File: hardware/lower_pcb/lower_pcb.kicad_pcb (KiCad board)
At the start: 2 copper layers, 88 x 88 mm, 22 parts, among them J1 USB-C, J2 JST-PH-2P, J3 FPC-6P-0.5mm, J4 Alps-RKJXV, SW1 MSK-12C02, SW2 BOOT-SW, SW3 RESET-SW, U1 XIAO-ESP32S3, U3 AP2112K-3.3V

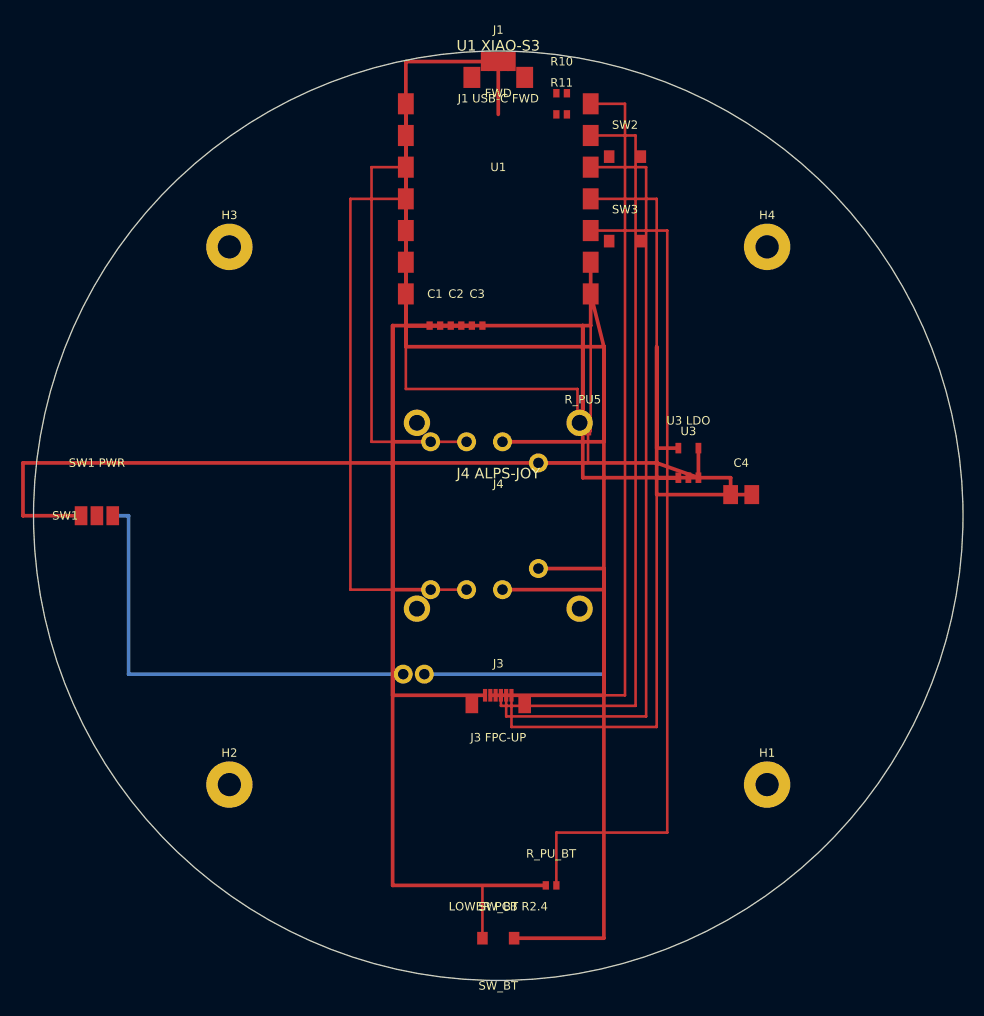
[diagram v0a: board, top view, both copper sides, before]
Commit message: feat: simplify to 2-layer single-sided routing, all traces on F.Cu
- All signal and power traces moved to F.Cu only
- No vias anywhere - eliminates layer-change complexity
- B.Cu = solid GND pour only (add zone fill in KiCad)
- BAT_PLUS routed on F.Cu around south edge to SW1
- J2 battery and J5 FPC connectors both on F.Cu (THT accessible both sides)
- Lower PCB: 88 segments (was 91 with vias/B.Cu traces)
- Upper PCB: 42 segments (was 52 with B.Cu vias)
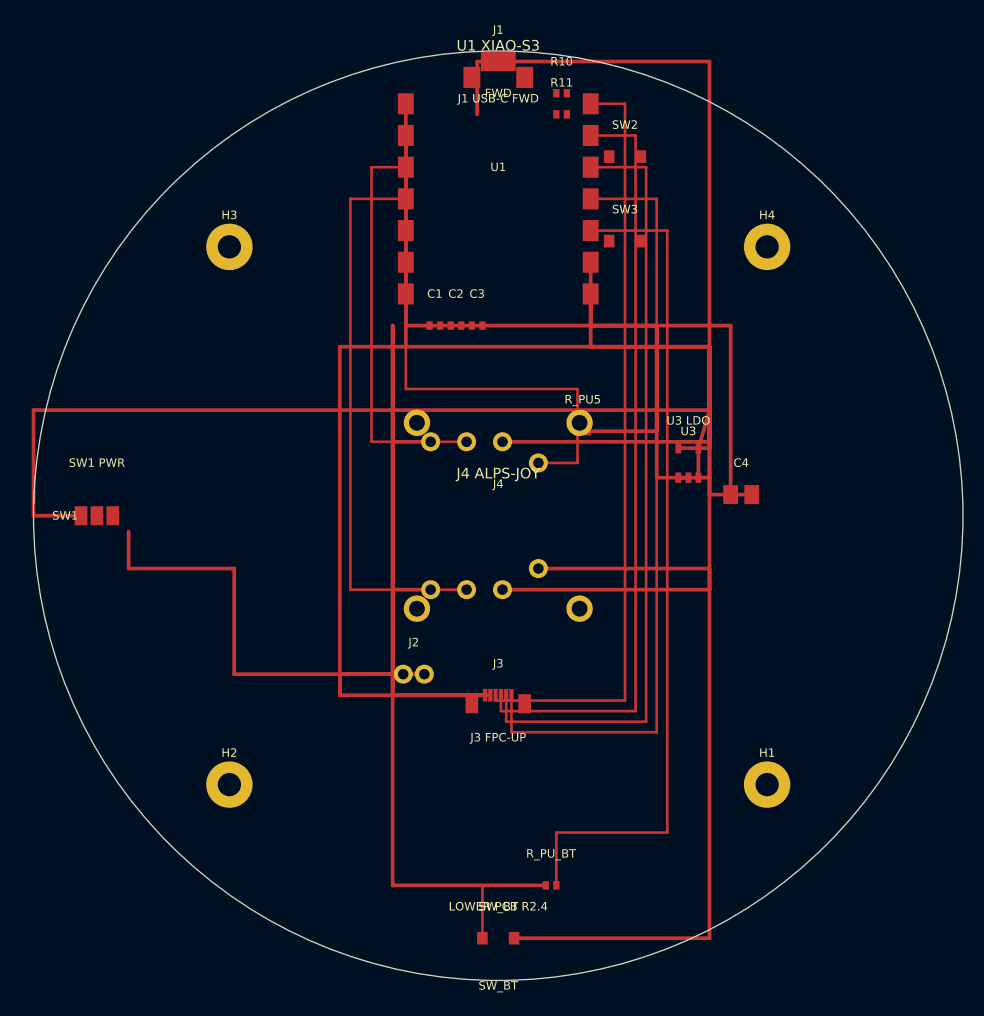
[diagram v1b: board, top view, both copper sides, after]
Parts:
- J2: moved to F.Cu
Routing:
- net GND: track 254.4 -> 349.3 mm, vias 1 -> 0
- net 3V3: track 210.9 -> 233.3 mm
- net JOY_SW: track 60.2 -> 42.0 mm
- net SW_OUT: track 77.5 -> 85.1 mm
- net BAT_PLUS: track 42.5 -> 39.5 mm
- net BTN_R: track 72.0 -> 73.0 mm
- net BTN_L: track 71.5 -> 72.5 mm
- net BTN_FW: track 73.0 -> 74.0 mm
- net BTN_BK: track 72.5 -> 73.5 mm
- net VBUS: track 6.25 -> 5.75 mm

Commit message: fix: rewrite add_traces.py with verified pad coordinates
All trace endpoints now match exact footprint pad positions:
- XIAO: 7 left pads + 7 right pads at correct absolute coords
- J4 Alps RKJXV: X/Y wipers, CCW(3V3), CW(GND), SW, mounting legs
- J3/J5 FPC: 6 signal pads at 0.5mm pitch
- U3 LDO SOT-23-5: pin1-5 exact positions
- J2 JST-PH: pin1(BAT+), pin2(GND)
- SW1 SPDT: COM/NO at correct rotated positions
- SW4/SW5 GM8.0: NO(-5.08)/COM(0)/NC(+5.08) horizontal row
- SW6/SW7 SKHLLBA010: 4 holes at +-3.25mm square
- R1-R4, R_PU5, R_PU_BT, C1-C4 pull-ups and decoupling
- 573 lower + 239 upper trace segments, all F.Cu, zero vias
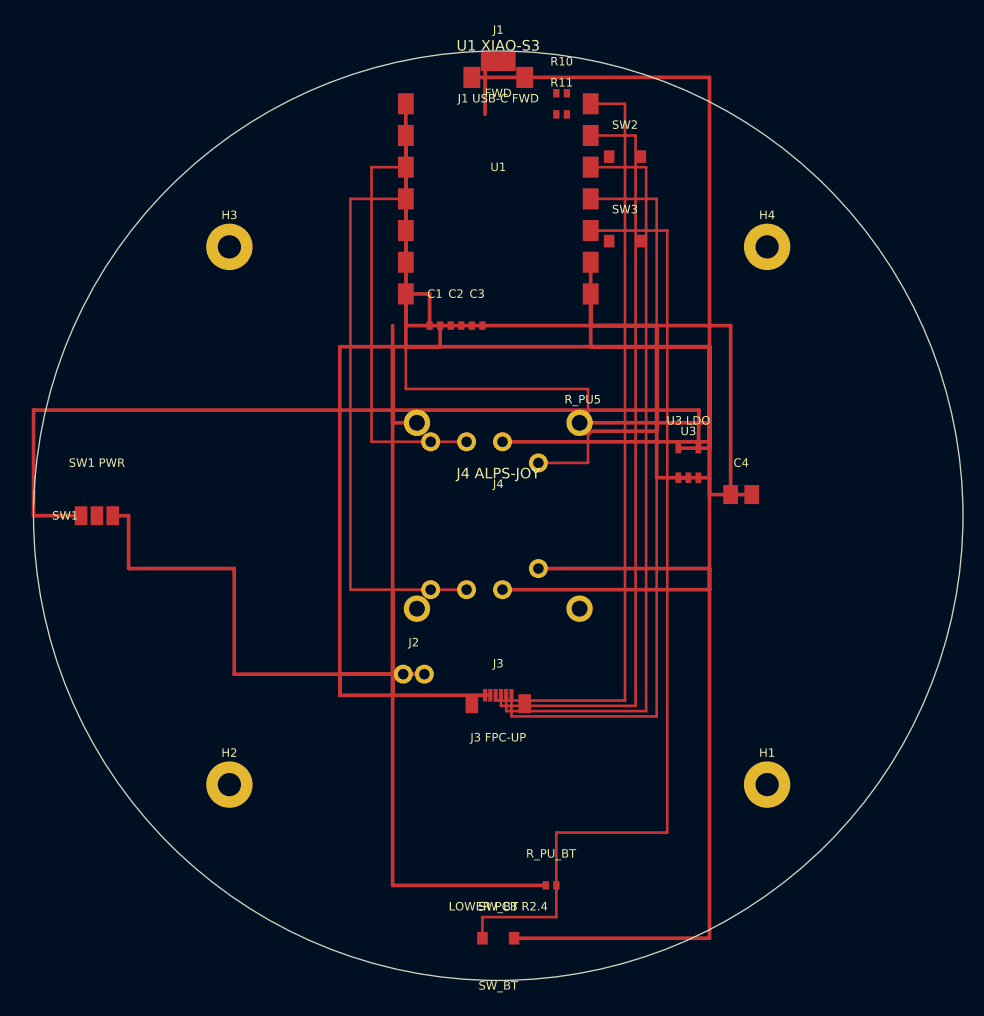
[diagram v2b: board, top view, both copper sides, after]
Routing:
- net GND: track 349.3 -> 385.1 mm
- net 3V3: track 233.3 -> 197.7 mm
- net SW_OUT: track 85.1 -> 81.1 mm
- net BTN_FW: track 74.0 -> 71.0 mm
- net BAT_PLUS: track 39.5 -> 42.5 mm
- net JOY_SW: track 42.0 -> 44.0 mm
- net BTN_BK: track 73.5 -> 71.5 mm
- net BT_SYNC: track 90.8 -> 91.8 mm
- net BTN_R: track 73.0 -> 72.0 mm
- net VBUS: track 5.75 -> 5.00 mm

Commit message: feat: replace generic XIAO with Seeed XIAO ESP32-S3 Sense footprint
- Correct castellated pad pitch: 2.54mm (was wrong 3.0mm)
- Correct pin count: 8 per side (was 7)
- GPIO remapping to actual XIAO ESP32-S3 Sense pin names:
    JOY_X  → D0/A0 (GPIO1)
    JOY_Y  → D1/A1 (GPIO2)
    JOY_SW → D2/A2 (GPIO3)
    ADC_BAT→ D3/A3 (GPIO4)
    BTN_L  → D10/MOSI (GPIO10)
    BTN_R  → D9/MISO (GPIO9)
    BTN_BK → D8/SCK (GPIO8)
    BTN_FW → D7/RX (GPIO44)
    BT_SYNC→ D6/TX (GPIO43)
    VIN/VBAT→ right pad 1 (from SW1 → J2 LiPo)
- Removed: J1 USB-C, U3 AP2112K LDO, R10/R11 CC, C4
  (all redundant — XIAO has built-in USB-C, charging IC, 3.3V LDO)
- Net list simplified: VBUS/BAT_PLUS/SW_OUT removed, VBAT added
- SW1 now switches VBAT directly to XIAO VIN
- Lower PCB rev 3.0
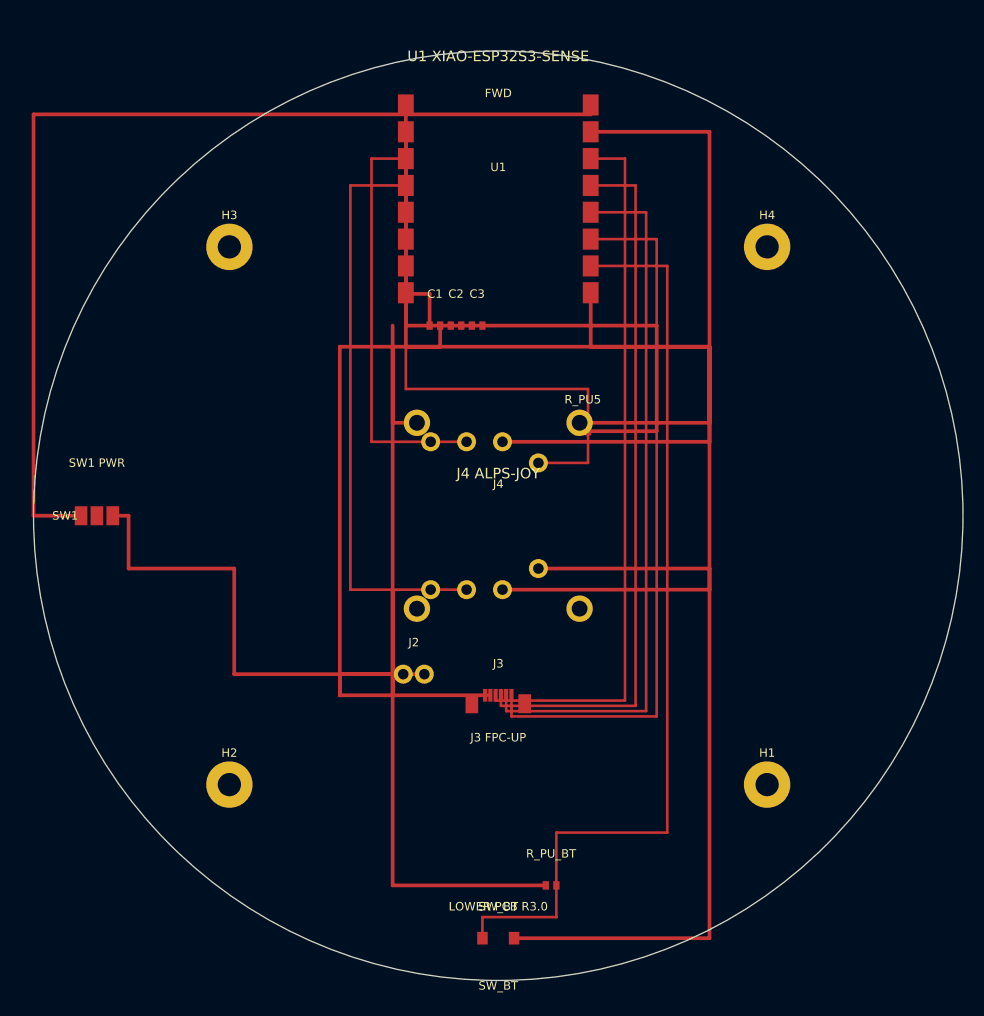
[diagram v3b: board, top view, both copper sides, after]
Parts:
- removed C4: C-0805, C4
- removed J1: USB-C, J1
- removed R10: R-0402, R10
- removed R11: R-0402, R11
- removed SW2: BOOT-SW, SW2
- removed SW3: RESET-SW, SW3
- removed U3: AP2112K-3.3V, U3
- U1: value XIAO-ESP32S3 -> Seeed-XIAO-ESP32S3
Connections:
- J2 pad 1: BAT_PLUS -> VBAT
- SW1 pad 1: BAT_PLUS -> VBAT
- SW1 pad 2: BAT_PLUS -> VBAT
- SW1 pad 3: SW_OUT -> VBAT
- U1 pad 1: 3V3 -> GND
- U1 pad 10: BTN_BK -> GND
- U1 pad 11: BTN_FW -> BTN_L
- U1 pad 12: BT_SYNC -> BTN_R
- U1 pad 13: 3V3 -> BTN_BK
- U1 pad 14: GND -> BTN_FW
- U1 pad 2: GND -> 3V3
- U1 pad 8: BTN_L -> GND
- U1 pad 9: BTN_R -> VBAT
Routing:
- net VBAT: track 0.00 -> 138.6 mm
- net SW_OUT: track 81.1 -> 0.00 mm
- net 3V3: track 197.7 -> 142.3 mm
- net GND: track 385.1 -> 338.2 mm
- net BAT_PLUS: track 42.5 -> 0.00 mm
- net BTN_L: track 72.5 -> 67.3 mm
- net VBUS: track 5.00 -> 0.00 mm
- net BTN_R: track 72.0 -> 67.3 mm
- net BTN_BK: track 71.5 -> 67.2 mm
- net BTN_FW: track 71.0 -> 67.2 mm
- net BT_SYNC: track 91.8 -> 88.4 mm
- net JOY_SW: track 44.0 -> 45.7 mm
- net JOY_Y: track 53.2 -> 54.5 mm
- net JOY_X: track 38.2 -> 39.1 mm
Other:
- board text added: "LOWER PCB R3.0"
- board text added: "U1 XIAO-ESP32S3-SENSE"
- board text removed: "J1 USB-C FWD"
- board text removed: "LOWER PCB R2.4"
- board text removed: "U1 XIAO-S3"
- board text removed: "U3 LDO"

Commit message: feat: replace generic XIAO with Seeed XIAO ESP32-S3 (Sense) lower PCB rev 3.0
- Seeed XIAO ESP32-S3 has built-in: USB-C, 3V3 LDO (1A), LiPo charger (SGM40567),
  BOOT and RESET buttons — removed external J1 USB-C, U3 LDO, SW1 power switch
- Correct 7-pad castellated footprint: 2.54mm pitch (not 3.0mm), 1.5x2.0mm pads
- XIAO pinout per Seeed wiki: L1-L7 and R1-R7, VBAT/GND back pads
- GPIO assignments: D0-D4(left) for JOY+ADC+BTN_L; D5-D8(right) for BTN_R/BK/FW+BT_SYNC
- LiPo J2 JST-PH routes directly to XIAO VBAT back pad
- Added R_DIV1/R_DIV2 100k voltage divider for battery ADC monitoring
- Net list simplified: GND/3V3/VBAT + 9 signal nets
- Lower PCB: 370 trace segments, all F.Cu
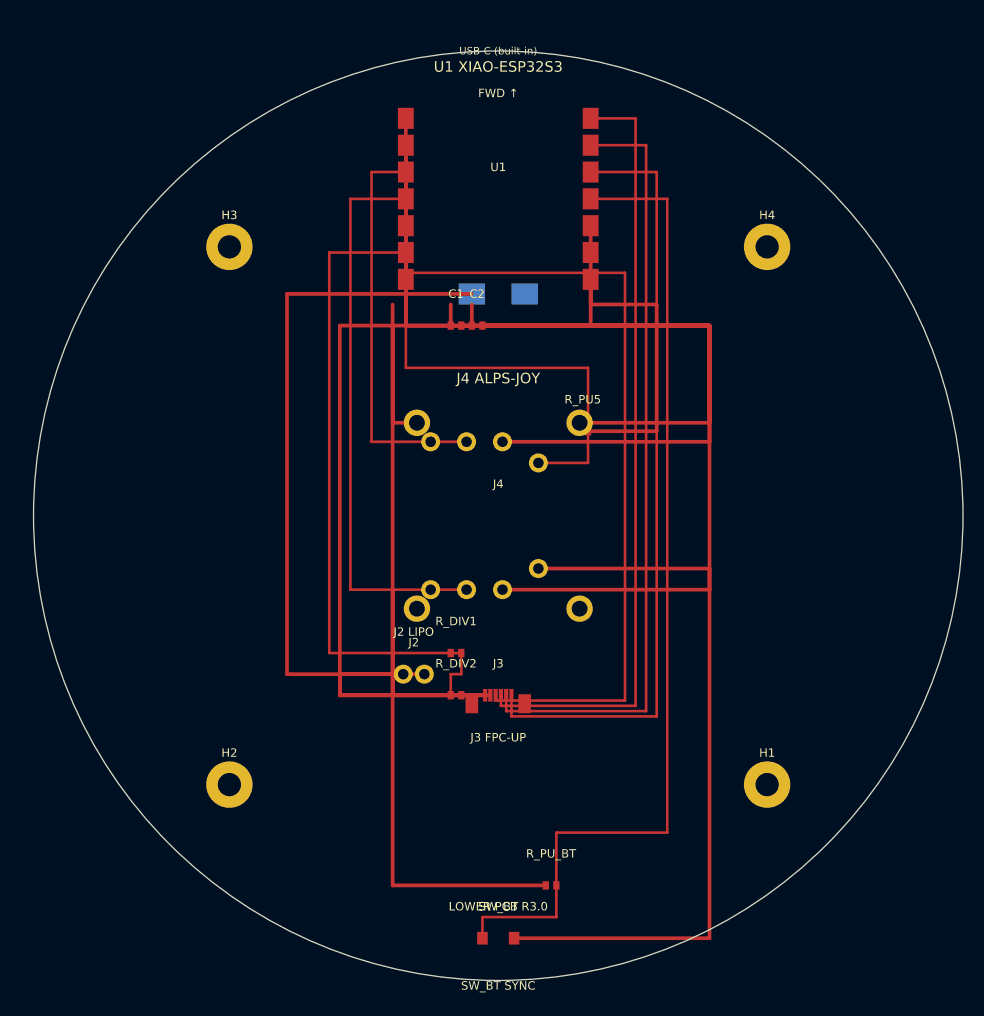
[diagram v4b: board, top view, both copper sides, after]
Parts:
- removed C3: R-0402, C3
- removed SW1: MSK-12C02, SW1
- added R_DIV1: R-0402, R_DIV1, F.Cu at (96.0, 113.0)
- added R_DIV2: R-0402, R_DIV2, F.Cu at (96.0, 117.0)
- moved C1 2.00 mm to (96.0, 82.0)
- moved C2 2.00 mm to (98.0, 82.0)
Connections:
- U1 pad 10: GND -> BTN_FW
- U1 pad 11: BTN_L -> BT_SYNC
- U1 pad 12: BTN_R -> GND
- U1 pad 13: BTN_BK -> GND
- U1 pad 14: BTN_FW -> 3V3
- U1 pad 15: BT_SYNC -> VBAT
- U1 pad 2: 3V3 -> GND
- U1 pad 7: GND -> BTN_L
- U1 pad 8: GND -> BTN_R
- U1 pad 9: VBAT -> BTN_BK
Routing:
- net GND: track 338.2 -> 414.8 mm
- net VBAT: track 138.6 -> 64.5 mm
- net ADC_BAT: track 0.00 -> 62.7 mm
- net 3V3: track 142.3 -> 120.4 mm
- net BTN_L: track 67.3 -> 74.6 mm
- net BTN_R: track 67.3 -> 73.6 mm
- net BTN_FW: track 67.2 -> 73.5 mm
- net BT_SYNC: track 88.4 -> 94.8 mm
- net BTN_BK: track 67.2 -> 73.6 mm
- net JOY_SW: track 45.7 -> 44.4 mm
- net JOY_Y: track 54.5 -> 53.2 mm
- net JOY_X: track 39.1 -> 37.8 mm
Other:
- board text added: "FWD ↑"
- board text added: "SW_BT SYNC"
- board text added: "U1 XIAO-ESP32S3"
- board text added: "USB-C (built-in)"
- board text removed: "FWD"
- board text removed: "SW1 PWR"
- board text removed: "SW_BT"
- board text removed: "U1 XIAO-ESP32S3-SENSE"

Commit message: feat: remove all traces (manual routing) + shrink silk labels
- add_traces.py is now a no-op — route in KiCad manually
- Lower PCB silk: all labels 0.6mm, shortened to fit within R44mm circle
- Upper PCB silk: all labels 0.5mm, shortened to fit within R27mm circle
- No functional changes to footprints or netlist
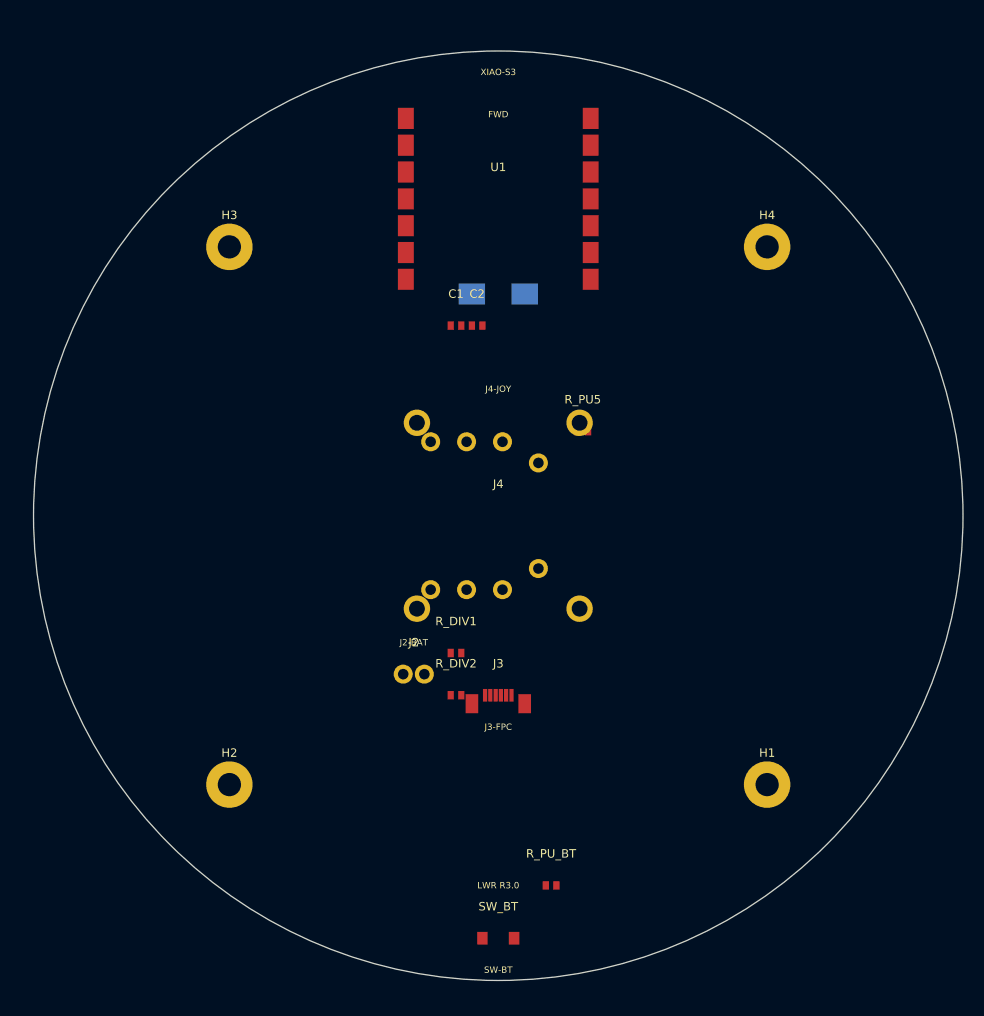
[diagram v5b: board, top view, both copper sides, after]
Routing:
- net GND: track 414.8 -> 0.00 mm
- net 3V3: track 120.4 -> 0.00 mm
- net BT_SYNC: track 94.8 -> 0.00 mm
- net BTN_L: track 74.6 -> 0.00 mm
- net BTN_R: track 73.6 -> 0.00 mm
- net BTN_BK: track 73.6 -> 0.00 mm
- net BTN_FW: track 73.5 -> 0.00 mm
- net VBAT: track 64.5 -> 0.00 mm
- net ADC_BAT: track 62.7 -> 0.00 mm
- net JOY_Y: track 53.2 -> 0.00 mm
- net JOY_SW: track 44.4 -> 0.00 mm
- net JOY_X: track 37.8 -> 0.00 mm
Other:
- board text added: "FWD"
- board text added: "J2-BAT"
- board text added: "J3-FPC"
- board text added: "J4-JOY"
- board text added: "LWR R3.0"
- board text added: "SW-BT"
- board text added: "XIAO-S3"
- board text removed: "FWD ↑"
- board text removed: "J2 LIPO"
- board text removed: "J3 FPC-UP"
- board text removed: "J4 ALPS-JOY"
- board text removed: "LOWER PCB R3.0"
- board text removed: "SW_BT SYNC"
- board text removed: "U1 XIAO-ESP32S3"
- board text removed: "USB-C (built-in)"
